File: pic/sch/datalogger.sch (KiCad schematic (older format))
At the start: 18 parts

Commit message: More schematic tweaks. Almost ready for PCB
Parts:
- added C? (x2): (22p), symbol C
- added C?: 220u, symbol CAPAPOL
- added C? (x2): 1u, symbol C
- added D?: LED_RG, symbol LED_RG
- added D?: 1n419, symbol DIODE
- added IC?: MCP1700T-3302ETT, symbol MCP1700T-3302ETT
- added P? (x3): JACK_LUMBERG_1503_13_VP3, symbol JACK_LUMBERG_1503_13_VP3
- added P?: CONN_2, symbol CONN_2
- added R? (x2): 330, symbol R
- added R? (x2): R, symbol R
- added X?: (16M), symbol CRYSTAL
- C?: value C -> 18p
- C?: value C -> 22p
- C?: value C -> 0.1u
- X?: value CRYSTAL -> 32.768k
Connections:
- net +3.3V: now also C?.1, D?.1 (A), IC?.2 (Vout), P?.4a, P?.4a, P?.4a, P?.4b, P?.4b, P?.4b; no longer IC?.8 (Vcc)
- net GND: now also C?.2, C?.2, C?.2, C?.2, C?.2, D?.3 (GND), IC?.1 (GND), P?.1, P?.1, P?.1, P?.2 (PM), R?.2
- net at IC?.10 (RA6/OSC2/CLKO): now also C?.1, X?.1
- net at IC?.12 (RC1/CCP2/P2A/SOSCI): now also R?.2
- net at IC?.13 (RC2/AN14/CTPLS/CCP1/P1A/T5CKI): now also R?.2
- net at IC?.2 (RA0/AN0/C12IN0-): now also P?.3
- net at IC?.21 (RB0/AN12/SRI/CCP4/FLT0/SS2/INT0), IC?.7 (MFP), R?.2: now also IC?.14 (CP2)
- net SCL: now reaches IC?.22 (RB1/AN10/C12IN3-/P1C/SCK2/INT1), IC?.6 (SCL), R?.2
- net SCL: now also P?.3
- net SDA: now reaches IC?.23 (RB2/AN8/CTED1/P1B/SDI2/SDA2/INT2), IC?.5 (SDA), R?.2
- net SDA: now also P?.2
- net at IC?.3 (RA1/AN1/C12IN1-): now also P?.2
- net at IC?.4 (RA2/AN2/C2IN+/Vref-/DACOUT): now also P?.3
- net at IC?.5 (RA3/AN3/C1IN+/Vref+): now also P?.2
- net at IC?.7 (RA5/AN4/C2OUT/SRNQ/HLVDIN/SS1): now also R?.1, R?.2
- net at IC?.9 (RA7/OSC1/CLKI): now also C?.1, X?.2
- new net: C?.1, D?.2 (K), IC?.8 (Vcc)
- new net: D?.1 (RED), R?.1
- new net: D?.2 (GRN), R?.1
- new net: C?.1, IC?.3 (Vin), P?.1 (P1), R?.1
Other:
- note added: "Battery input\n3 x AA cells\n3.6-4.5VDC"
- moved on the sheet: C?, IC?, P?, R?, X?

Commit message: Schematic more or less finished.
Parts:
- added P5, P6: CONN_3, symbol CONN_3
- added Q1, Q2, Q3: 2N7002E, symbol 2N7002E
- added SW1: SW_PUSH4, symbol SW_PUSH4
- R1, R2: renamed from R?; value R -> 10k
- gave numbers to parts that had none: 33
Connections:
- net labels added: +BATT, PWR1, PWR2
- wire segments 148 -> 182
- no-connect marks 5 -> 8
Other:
- moved on the sheet: C1, C4, C6, D1, IC1, P1, P2, P3, P4, P7, R1, R2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

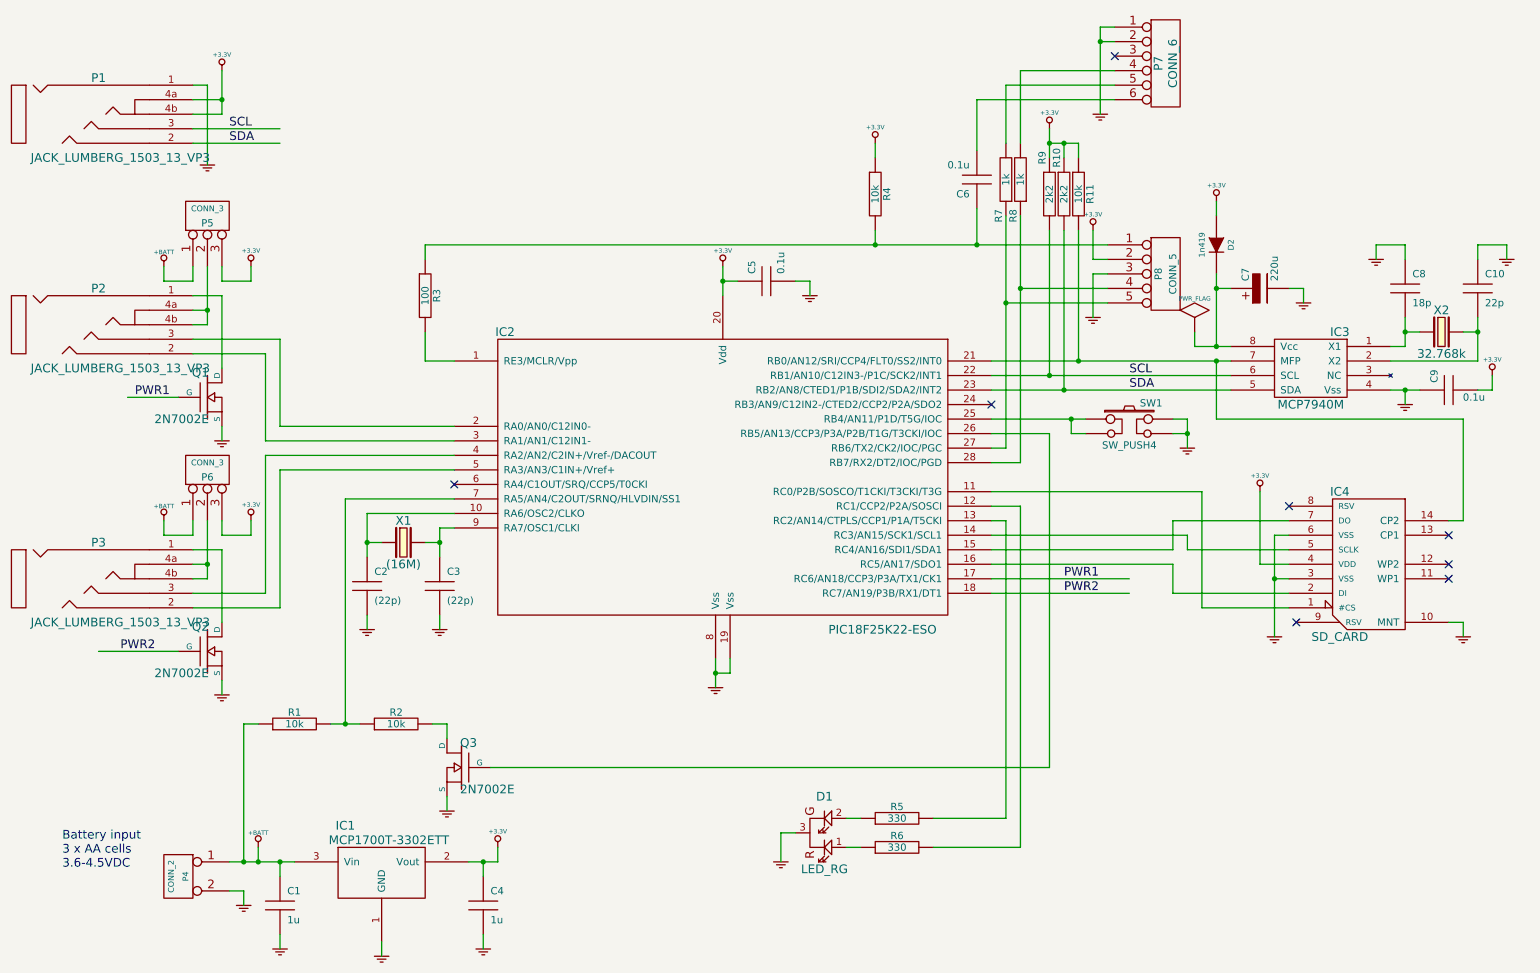
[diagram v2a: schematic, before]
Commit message: PCB layout first pass done.  Needs some tidying.
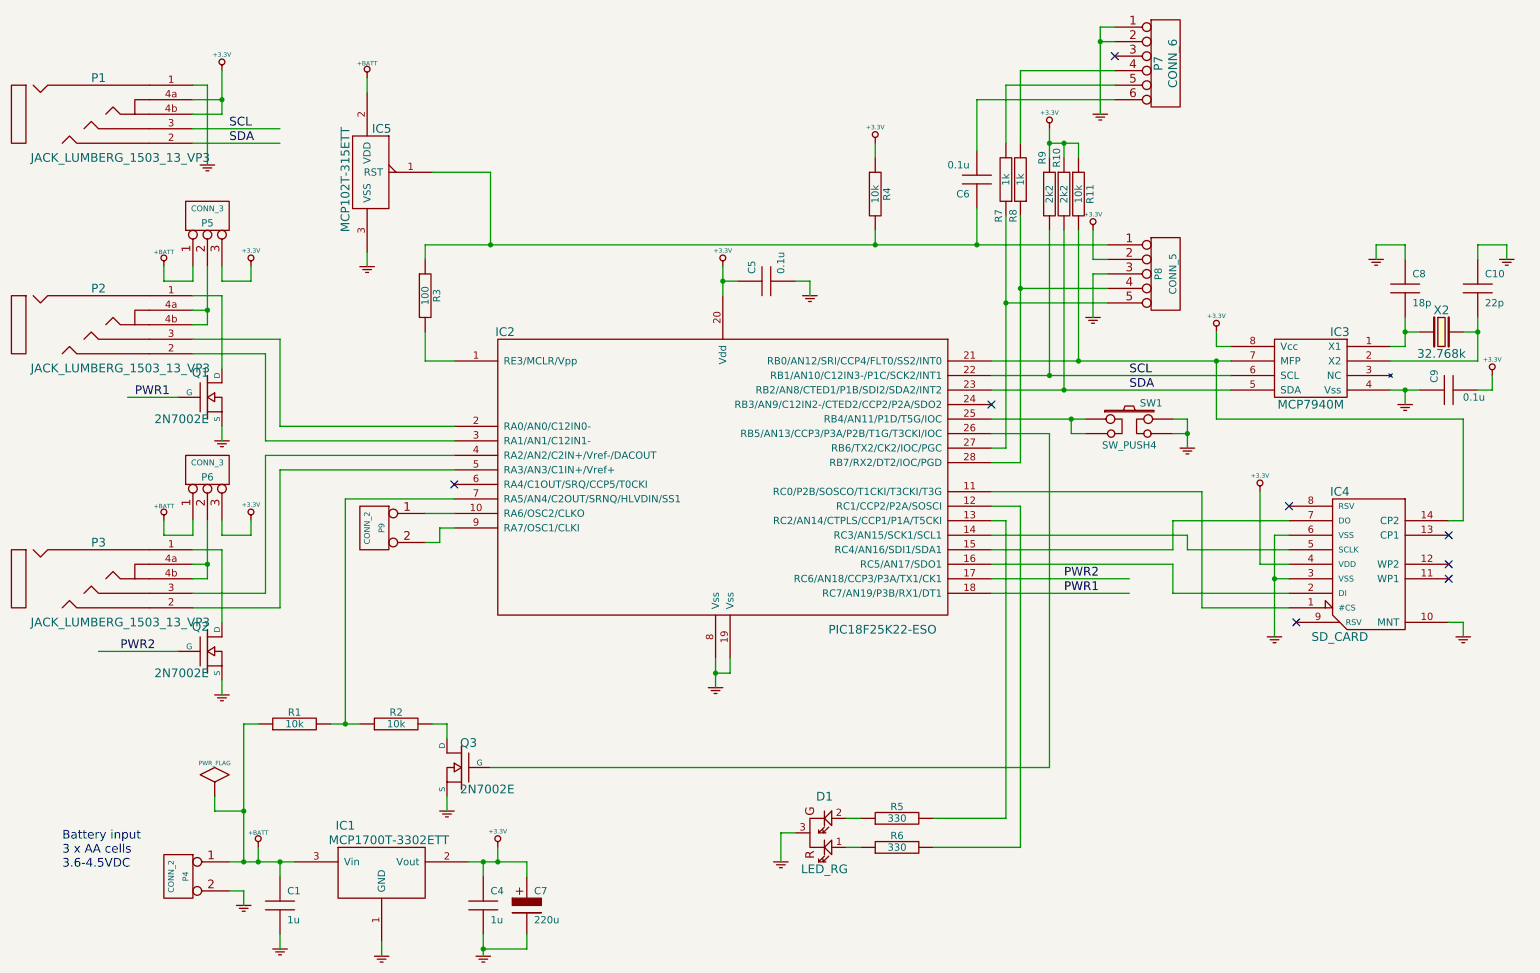
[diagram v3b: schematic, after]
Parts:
- removed C2, C3: (22p), symbol C
- removed D2: 1n419, symbol DIODE
- removed X1: (16M), symbol CRYSTAL
- added IC5: MCP102T-315ETT, symbol MCP102T-315ETT
- added P9: CONN_2, symbol CONN_2
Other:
- moved on the sheet: C7
